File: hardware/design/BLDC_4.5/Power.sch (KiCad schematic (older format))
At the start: 74 parts, among them P4 IN+, P5 IN-, P6 MOTOR1, P7 MOTOR2, P9 MOTOR3, Q1 IRFS3006, Q2 IRFS3006, Q3 IRFS3006, Q4 IRFS3006, Q5 IRFS3006, Q6 IRFS3006, U2 NCP1117ST33T3G, U3 DRV8302

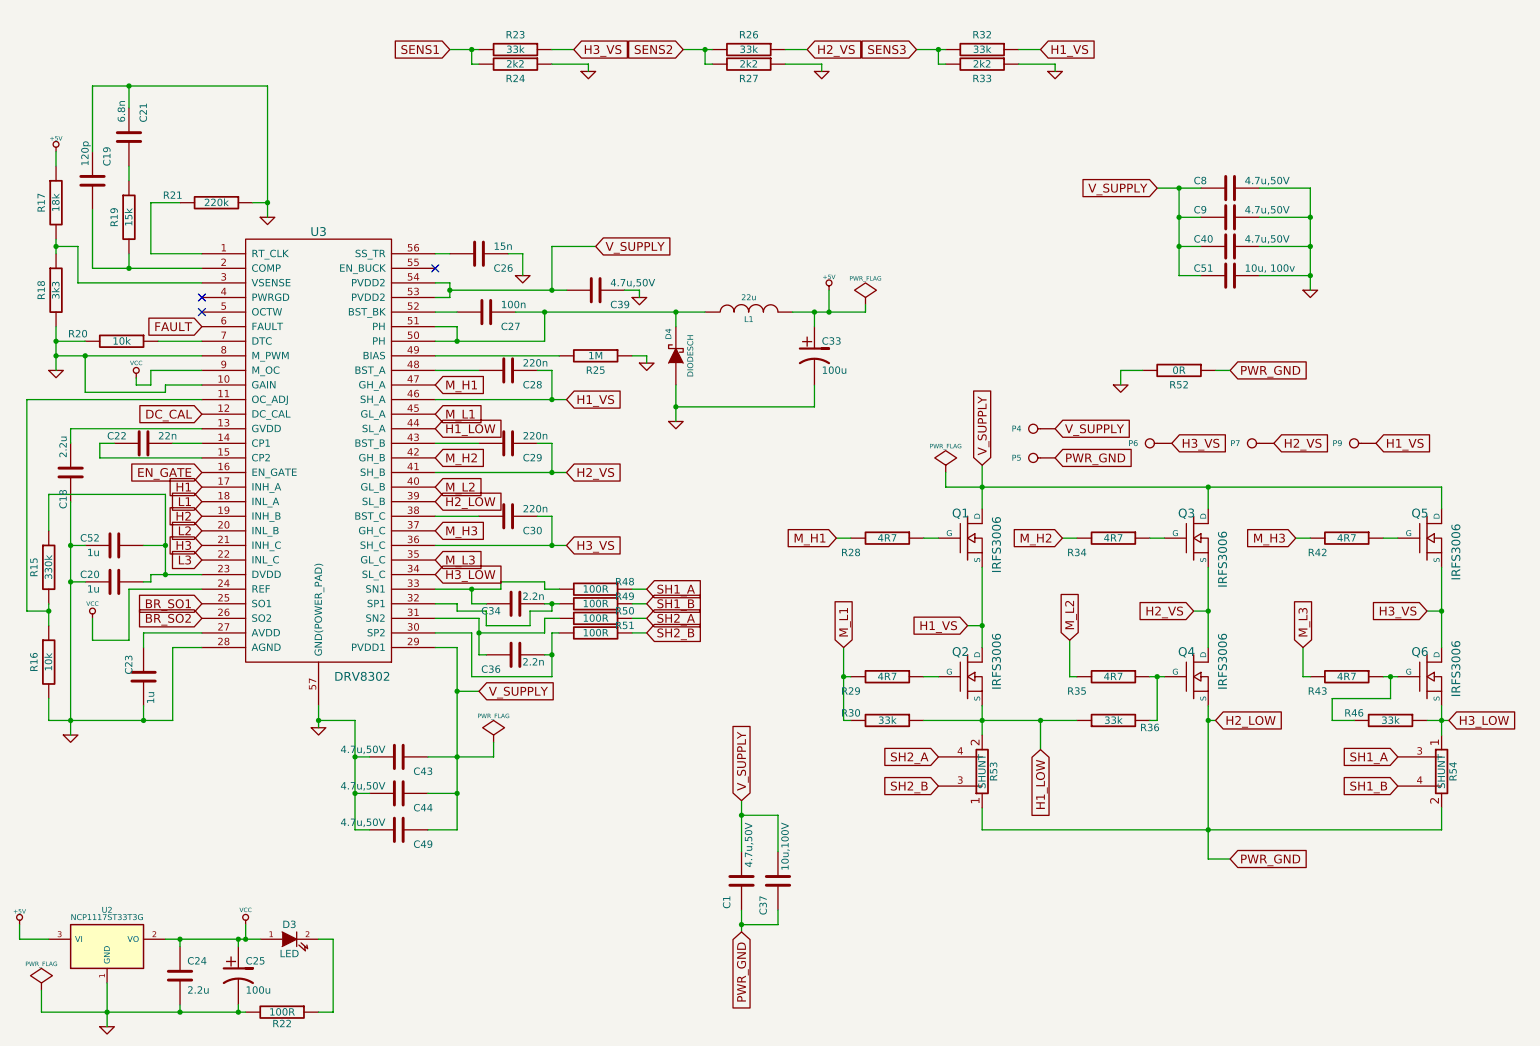
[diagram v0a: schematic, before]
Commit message: Schematic divided into 3 sheets to show a simpler top level flow. Added several images and general documentation
Signed-off-by: Marcos Chaparro <marcos@mrkindustries.com.ar>
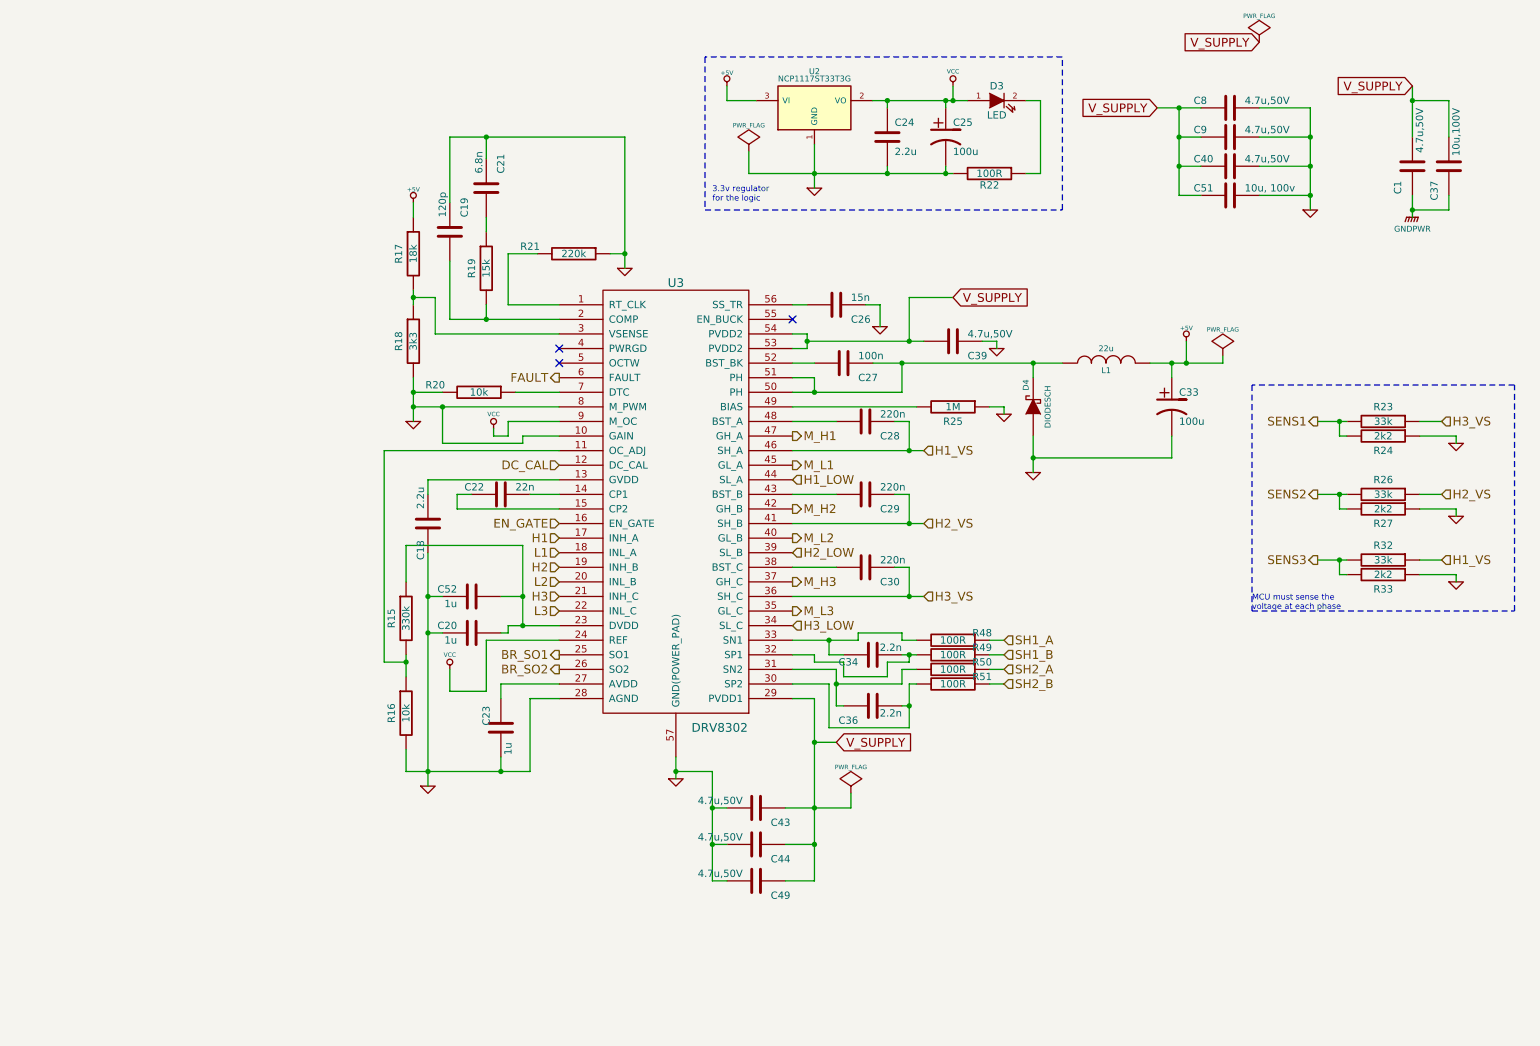
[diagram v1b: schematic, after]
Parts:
- removed P4: IN+, symbol CONN_1
- removed P5: IN-, symbol CONN_1
- removed P6: MOTOR1, symbol CONN_1
- removed P7: MOTOR2, symbol CONN_1
- removed P9: MOTOR3, symbol CONN_1
- removed Q1, Q2, Q3, Q4, Q5, Q6: IRFS3006, symbol MOSFET_N
- removed R28, R29, R34, R35, R42, R43: 4R7, symbol R
- removed R30, R36, R46: 33k, symbol R
- removed R52: 0R, symbol R
- removed R53, R54: SHUNT, symbol SHUNT
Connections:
- net H2_LOW: no longer C1.1, C37.1
- new net GNDPWR: C1.1, C37.1
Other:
- note added: "3.3v regulator\nfor the logic"
- note added: "MCU must sense the\nvoltage at each phase"
- moved on the sheet: C1, C18, C19, C20, C21, C22, C23, C24, C25, C26, C27, C28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

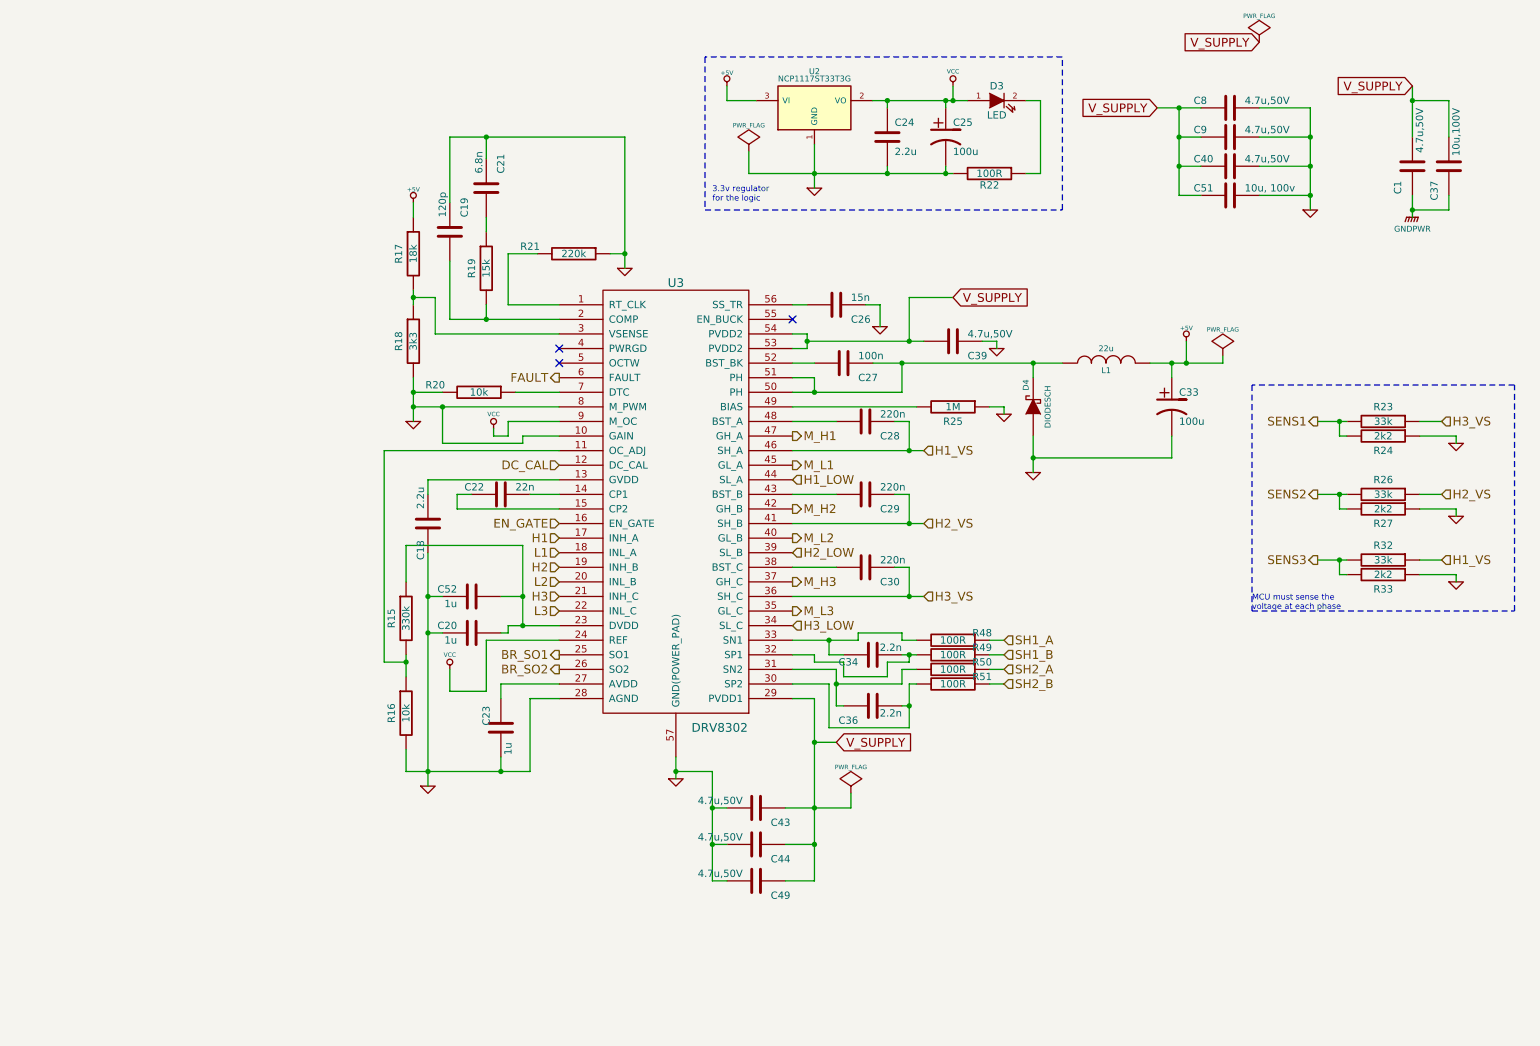
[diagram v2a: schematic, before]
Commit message: Schematic changes: Cleaner top level, added CAN connector, moved LEDs to top level, added 22 Ohm resistors for the USB lines. Fully annotated schematic, ready for layout.
Signed-off-by: Marcos Chaparro <marcos@mrkindustries.com.ar>
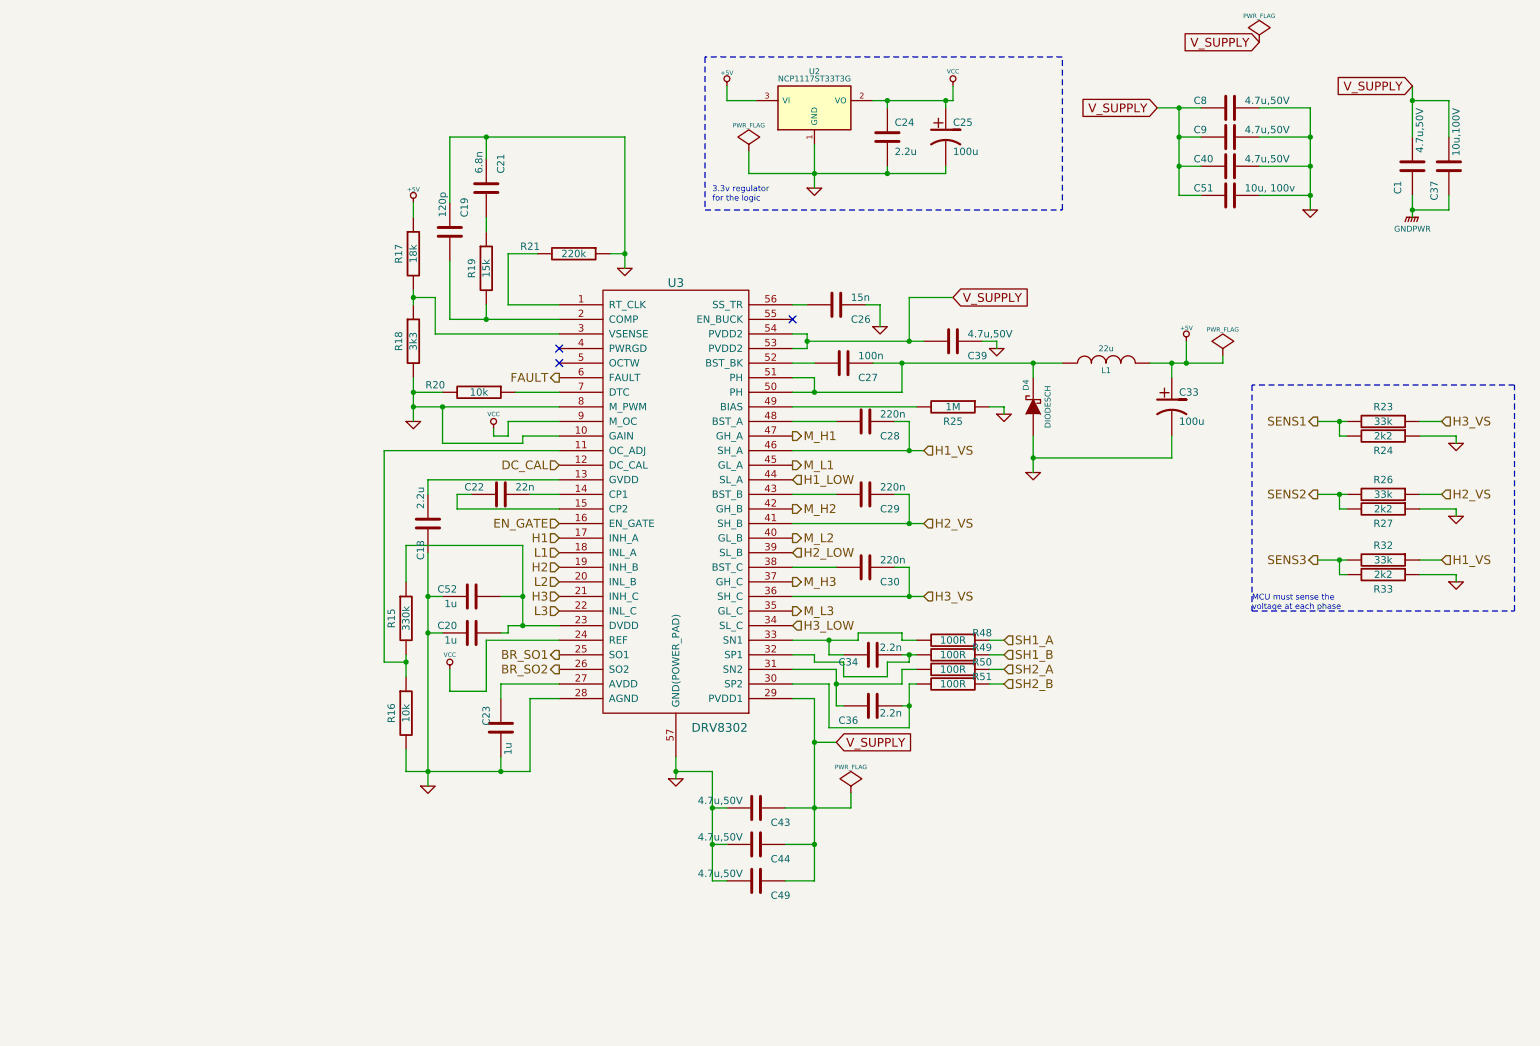
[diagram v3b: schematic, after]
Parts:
- removed D3: LED, symbol LED
- removed R22: 100R, symbol R

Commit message: Layout updated. Added inner power planes, changed USB connector, added CAN transceiver and connector, added 3D models copper pour under the mosfets and references moved to visible places
Signed-off-by: Marcos Chaparro <marcos@mrkindustries.com.ar>
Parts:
- C1, C39, C40, C43, C44, C49, C8, C9: footprint (none) -> SMD_Packages:SMD-1206
- C18, C23, C28, C29, C30: footprint (none) -> SMD_Packages:SMD-0805
- C19, C20, C21, C22, C24, C26, C27, C34, C36, C52: footprint (none) -> SMD_Packages:SMD-0603_c
- C25, C33: footprint (none) -> w_smd_cap:c_tant_B
- C37, C51: footprint (none) -> w_smd_cap:c_2220
- D4: footprint (none) -> Diodes_SMD:Diode-SMA_Handsoldering
- L1: footprint (none) -> w_smd_inductors:inductor_smd_8x5mm
- R15, R16, R17, R18, R19, R20, R21, R23, R24, R25, R26, R27, R32, R33, R48, R49, R50, R51: footprint (none) -> SMD_Packages:SMD-0603_r
- U2: footprint (none) -> SMD_Packages:SOT-223
- U3: footprint (none) -> CRF1:TSSOP-56-PP
